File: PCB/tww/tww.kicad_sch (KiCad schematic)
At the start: 53 parts, among them J1 MAINS, J10 Flow|NTC, J11 SPI, J2 WW_Pump, J3 Circ_Pump, J6 FtdiConnector, J9 1Wire Sensors, Q1 BC547, Q2 BC547, SW1 Reset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

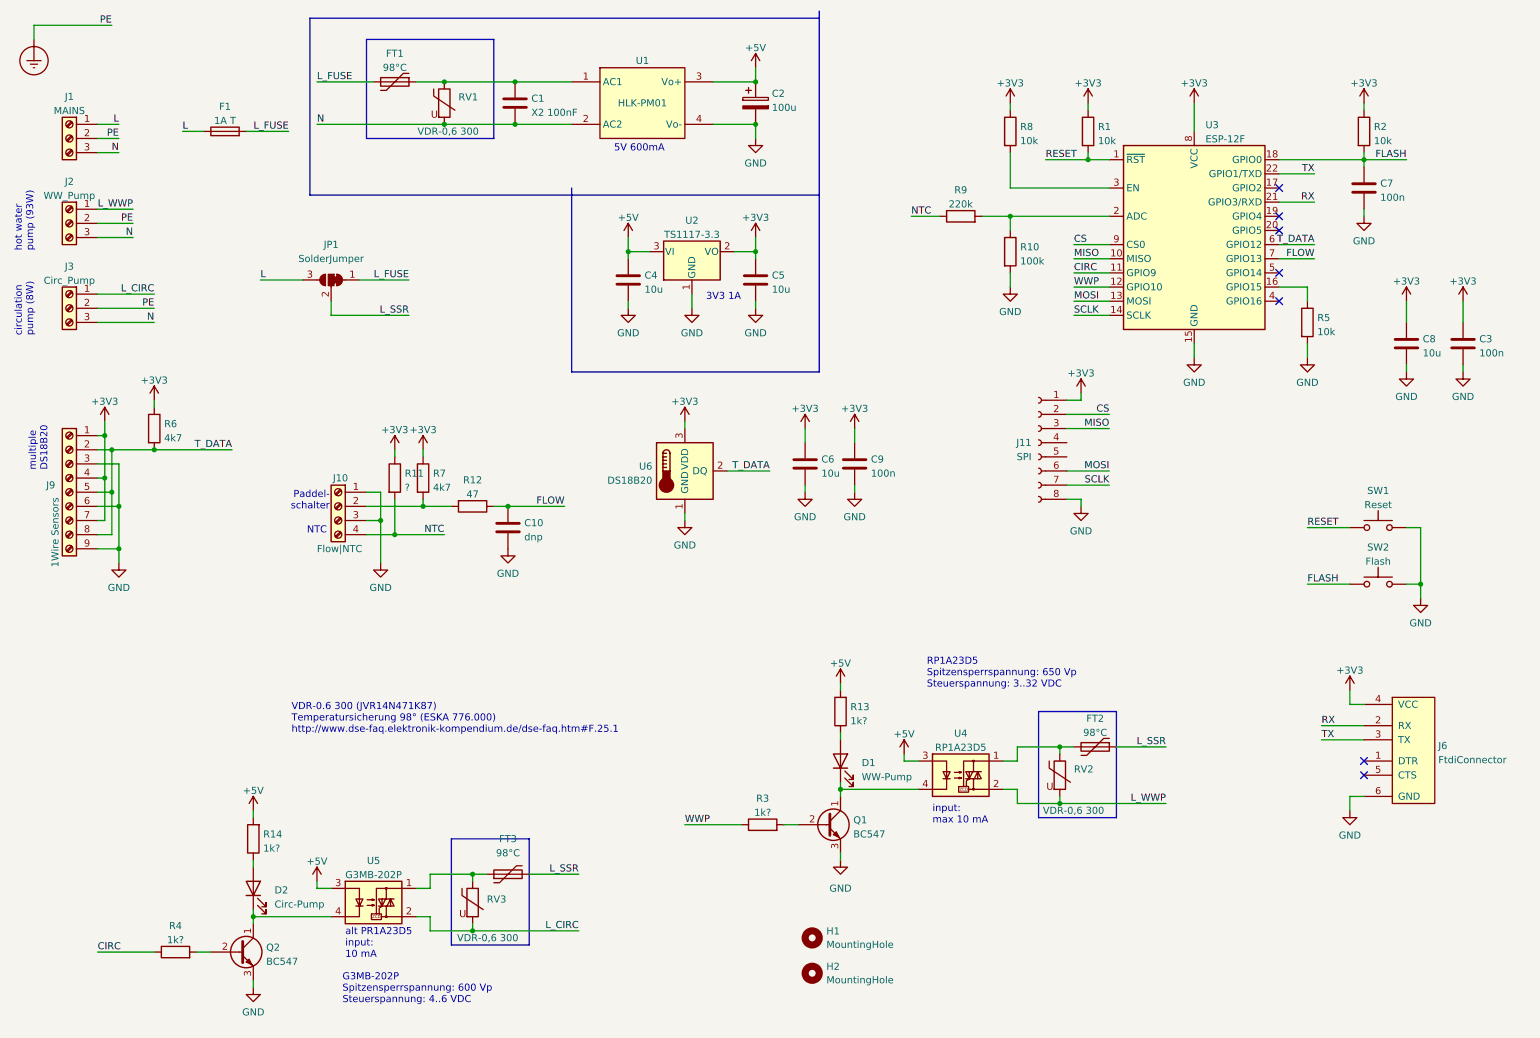
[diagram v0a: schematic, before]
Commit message: update to PCB v1.1
addresses #1

- U1 (HLK-PM01) output polarity swapped
- J6 (FtdiConnector): RX and TX swapped
- J10 label fixed
- VDR-0.6 footprint changed
- replaced BC547 by FET IRLML6344
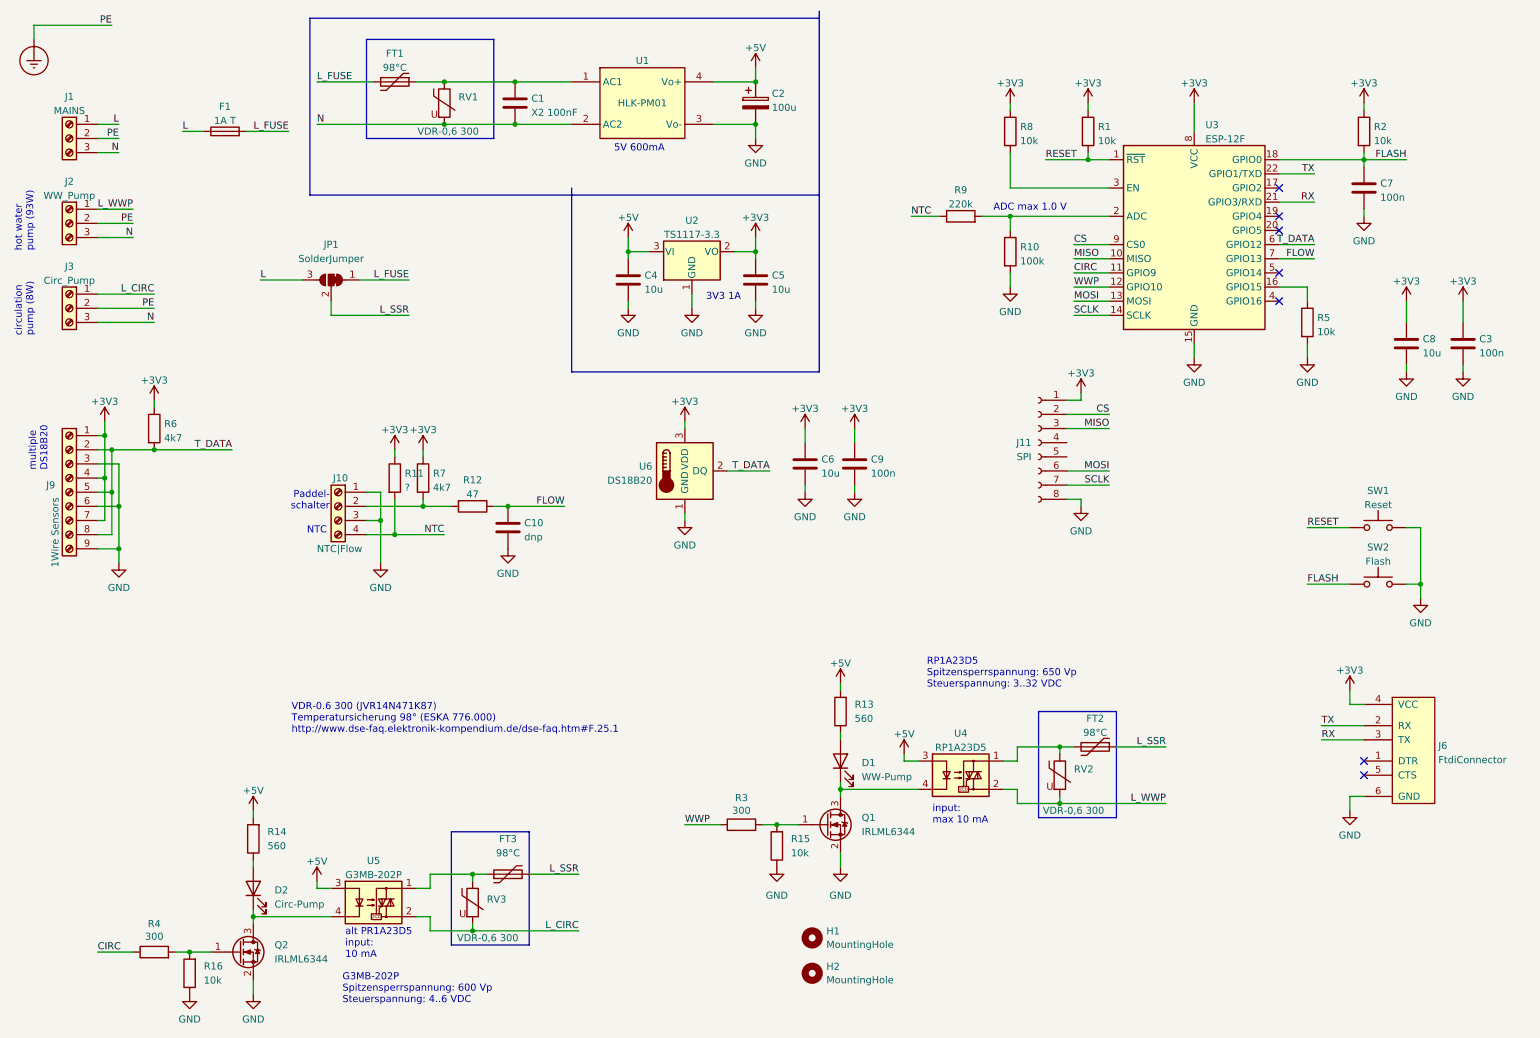
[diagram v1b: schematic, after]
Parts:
- removed Q1, Q2: BC547, Package_TO_SOT_THT:TO-92_Inline, symbol Transistor_BJT:BC547
- added Q1, Q2: IRLML6344, Package_TO_SOT_SMD:SOT-23_Handsoldering, symbol Transistor_FET:IRLML2060
- added R15, R16: 10k, Resistor_SMD:R_0805_2012Metric_Pad1.20x1.40mm_HandSolder, symbol Device:R
- J10: value Flow|NTC -> NTC|Flow
- R13, R14: value 1k? -> 560
- R3, R4: value 1k? -> 300
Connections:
- net +5V: now also U1.4 (Vo+); no longer U1.3 (Vo+)
- net GND: now also U1.3 (Vo-), Q1.2 (S), Q2.2 (S), R15.1, R16.1; no longer U1.4 (Vo-)
- net RX: now also J6.3 (TX); no longer J6.2 (RX)
- net TX: now also J6.2 (RX); no longer J6.3 (TX)
- net at D1.1 (K), U4.4: now also Q1.3 (D)
- net at R3.2: now also Q1.1 (G), R15.2
- net at D2.1 (K), U5.4: now also Q2.3 (D)
- net at R4.2: now also Q2.1 (G), R16.2
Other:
- note added: "ADC max 1.0 V"
- moved on the sheet: R3, R4

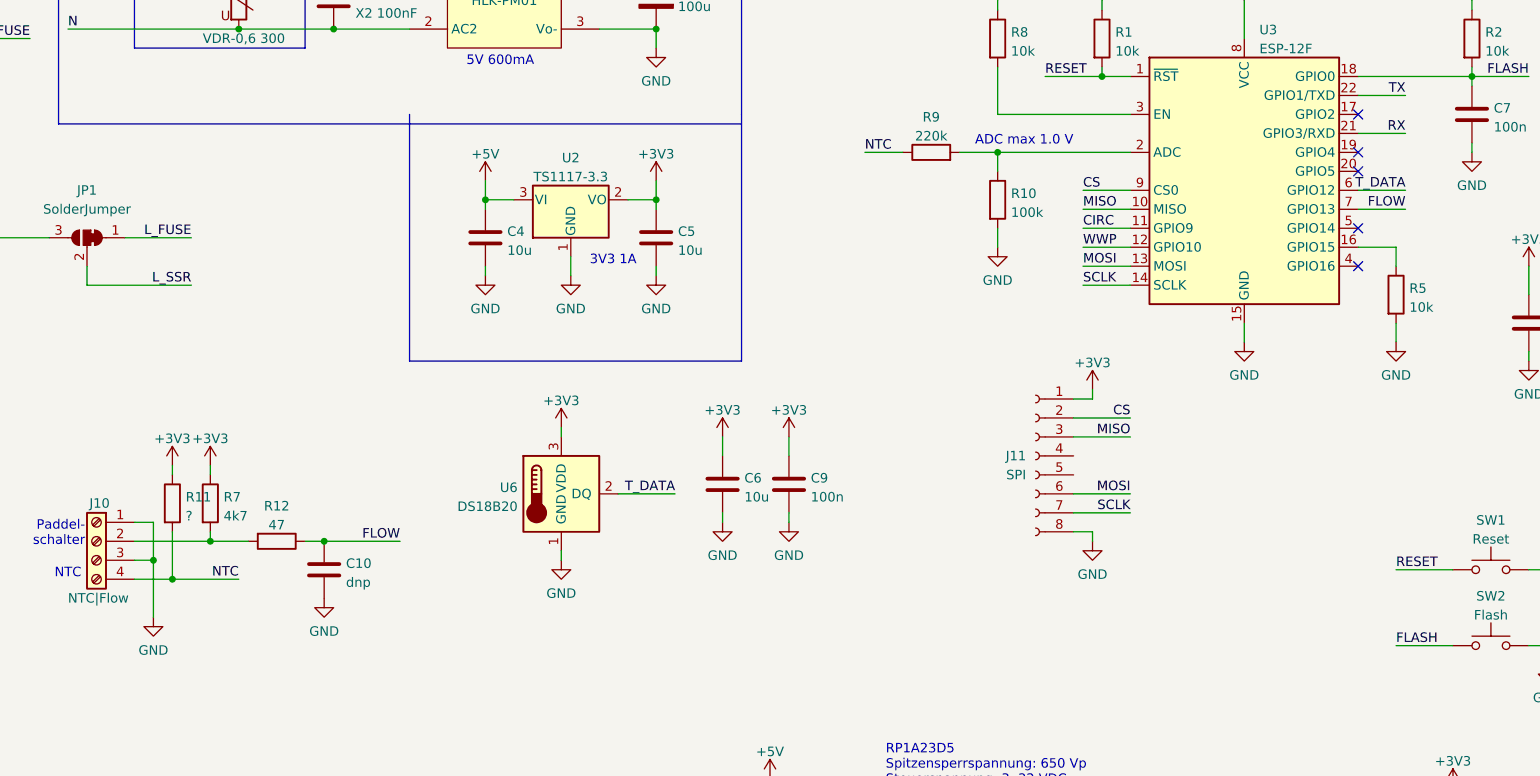
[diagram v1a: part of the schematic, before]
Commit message: updates for PCB version 1.1
- reconnect WWP and CIRC outputs
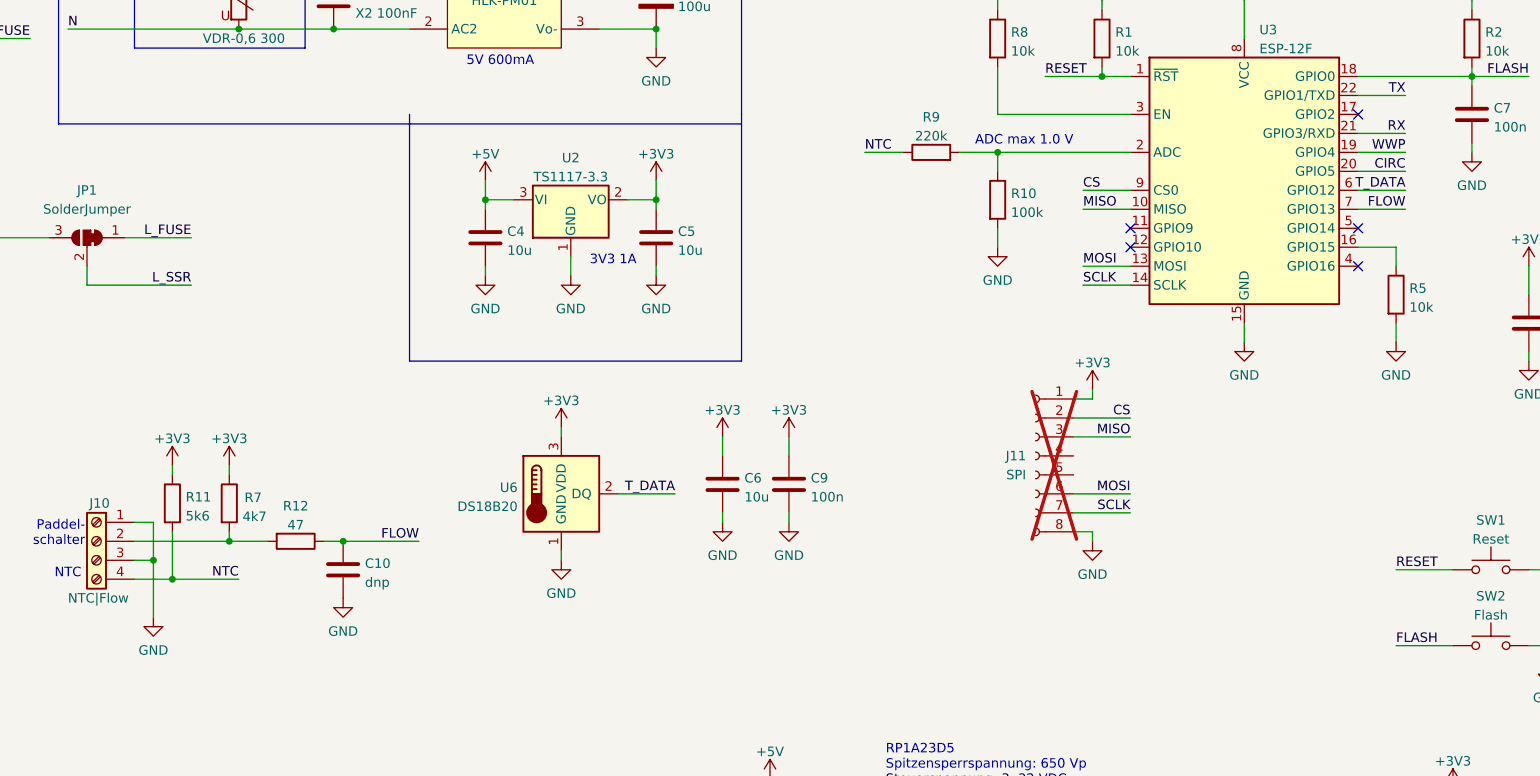
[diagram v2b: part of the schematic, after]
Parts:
- J11: now not fitted
- R11: value ? -> 5k6
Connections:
- net CIRC: now also U3.20 (GPIO5); no longer U3.11 (GPIO9)
- net WWP: now also U3.19 (GPIO4); no longer U3.12 (GPIO10)
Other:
- moved on the sheet: C10, R12, R7
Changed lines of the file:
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@@
 	(title_block
 		(title "TWW - Trinkwarmwasser")
-		(date "2024-10-22")
+		(date "2024-11-15")
 		(rev "1.1")
 		(comment 1 "CC BY-NC-SA 4.0")
@@
 	)
 	(junction
-		(at 104.14 104.14)
+		(at 106.68 104.14)
 		(diameter 0)
 		(color 0 0 0 0)
@@
 	)
 	(junction
+		(at 91.44 104.14)
+		(diameter 0)
+		(color 0 0 0 0)
+	)
+	(junction
 		(at 148.59 35.56)
 		(diameter 0)
@@
 	)
 	(junction
-		(at 88.9 104.14)
-		(diameter 0)
-		(color 0 0 0 0)
-	)
-	(junction
 		(at 34.29 111.76)
 		(diameter 0)
@@
 	)
 	(no_connect
-		(at 242.57 54.61)
-	)
-	(no_connect
 		(at 257.81 152.4)
 	)
@@
 	)
 	(no_connect
-		(at 242.57 52.07)
+		(at 242.57 67.31)
 	)
 	(no_connect
-		(at 242.57 67.31)
+		(at 212.09 62.23)
 	)
 	(no_connect
@@
 		(at 242.57 46.99)
 	)
+	(no_connect
+		(at 212.09 64.77)
+	)
 	(wire
 		(pts
@@
 	(wire
 		(pts
-			(xy 205.74 62.23) (xy 212.09 62.23)
-		)
-		(stroke
-			(width 0)
-			(type default)
-		)
-	)
-	(wire
-		(pts
 			(xy 195.58 157.48) (xy 203.2 157.48)
 		)
@@
 	(wire
 		(pts
+			(xy 242.57 54.61) (xy 248.92 54.61)
+		)
+		(stroke
+			(width 0)
+			(type default)
+		)
+	)
+	(wire
+		(pts
 			(xy 97.79 170.18) (xy 100.33 170.18)
 		)
@@
 	(wire
 		(pts
-			(xy 205.74 64.77) (xy 212.09 64.77)
-		)
-		(stroke
-			(width 0)
-			(type default)
-		)
-	)
-	(wire
-		(pts
 			(xy 257.81 40.64) (xy 257.81 41.91)
 		)
@@
 	(wire
 		(pts
-			(xy 88.9 104.14) (xy 88.9 102.87)
+			(xy 91.44 104.14) (xy 91.44 102.87)
 		)
 		(stroke
@@
 	(wire
 		(pts
-			(xy 101.6 104.14) (xy 104.14 104.14)
+			(xy 104.14 104.14) (xy 106.68 104.14)
 		)
 		(stroke
@@
 	(wire
 		(pts
-			(xy 88.9 104.14) (xy 93.98 104.14)
-		)
-		(stroke
-			(width 0)
-			(type default)
-		)
-	)
-	(wire
-		(pts
 			(xy 242.57 57.15) (xy 248.92 57.15)
 		)
@@
 	(wire
 		(pts
-			(xy 88.9 93.98) (xy 88.9 95.25)
+			(xy 91.44 93.98) (xy 91.44 95.25)
 		)
 		(stroke
@@
 	(wire
 		(pts
+			(xy 242.57 52.07) (xy 248.92 52.07)
+		)
+		(stroke
+			(width 0)
+			(type default)
+		)
+	)
+	(wire
+		(pts
 			(xy 247.65 74.93) (xy 247.65 77.47)
 		)
@@
 	(wire
 		(pts
+			(xy 91.44 104.14) (xy 96.52 104.14)
+		)
+		(stroke
+			(width 0)
+			(type default)
+		)
+	)
+	(wire
+		(pts
 			(xy 30.48 93.98) (xy 33.02 93.98)
 		)
@@
 	(wire
 		(pts
-			(xy 104.14 104.14) (xy 114.3 104.14)
+			(xy 106.68 104.14) (xy 116.84 104.14)
 		)
 		(stroke
@@
 	(wire
 		(pts
-			(xy 78.74 104.14) (xy 88.9 104.14)
+			(xy 78.74 104.14) (xy 91.44 104.14)
 		)
 		(stroke
@@
 	)
 	(label "CIRC"
-		(at 205.74 62.23 0)
+		(at 248.92 54.61 180)
 		(fields_autoplaced yes)
 		(effects
@@
 				(size 1.27 1.27)
 			)
-			(justify left bottom)
+			(justify right bottom)
 		)
 	)
@@
 	)
 	(label "FLOW"
-		(at 114.3 104.14 180)
+		(at 116.84 104.14 180)
 		(fields_autoplaced yes)
 		(effects
@@
 	)
 	(label "WWP"
-		(at 205.74 64.77 0)
+		(at 248.92 52.07 180)
 		(fields_autoplaced yes)
 		(effects
@@
 				(size 1.27 1.27)
 			)
-			(justify left bottom)
+			(justify right bottom)
 		)
 	)
@@
 	(symbol
 		(lib_id "power:GND")
-		(at 104.14 111.76 0)
+		(at 106.68 111.76 0)
 		(unit 1)
 		(exclude_from_sim no)
@@
 		(fields_autoplaced yes)
 		(property "Reference" "#PWR033"
-			(at 104.14 118.11 0)
+			(at 106.68 118.11 0)
 			(effects
 				(font
@@
 		)
 		(property "Value" "GND"
-			(at 104.14 116.2034 0)
+			(at 106.68 116.2034 0)
 			(effects
 				(font
@@
 		)
 		(property "Footprint" ""
-			(at 104.14 111.76 0)
+			(at 106.68 111.76 0)
 			(effects
 				(font
@@
 		)
 		(property "Datasheet" ""
-			(at 104.14 111.76 0)
+			(at 106.68 111.76 0)
 			(effects
 				(font
@@
 		)
 		(property "Description" ""
-			(at 104.14 111.76 0)
+			(at 106.68 111.76 0)
 			(effects
 				(font
@@
 	(symbol
 		(lib_id "Device:C")
-		(at 104.14 107.95 0)
+		(at 106.68 107.95 0)
 		(unit 1)
 		(exclude_from_sim no)
@@
 		(dnp no)
 		(property "Reference" "C10"
-			(at 107.061 107.1153 0)
+			(at 109.601 107.1153 0)
 			(effects
 				(font
@@
 		)
 		(property "Value" "dnp"
-			(at 107.061 109.6522 0)
+			(at 109.601 109.6522 0)
 			(effects
 				(font
@@
 		)
 		(property "Footprint" "Capacitor_SMD:C_0805_2012Metric_Pad1.18x1.45mm_HandSolder"
-			(at 105.1052 111.76 0)
+			(at 107.6452 111.76 0)
 			(effects
 				(font
@@
 		)
 		(property "Datasheet" "~"
-			(at 104.14 107.95 0)
+			(at 106.68 107.95 0)
 			(effects
 				(font
@@
 		)
 		(property "Description" ""
-			(at 104.14 107.95 0)
+			(at 106.68 107.95 0)
 			(effects
 				(font
@@
 			)
 		)
-		(property "Value" "?"
+		(property "Value" "5k6"
 			(at 85.598 100.7622 0)
 			(effects
@@
 	(symbol
 		(lib_id "power:+3V3")
-		(at 88.9 93.98 0)
+		(at 91.44 93.98 0)
 		(unit 1)
 		(exclude_from_sim no)
@@
 		(fields_autoplaced yes)
 		(property "Reference" "#PWR0104"
-			(at 88.9 97.79 0)
+			(at 91.44 97.79 0)
 			(effects
 				(font
@@
 		)
 		(property "Value" "+3V3"
-			(at 88.9 90.4042 0)
+			(at 91.44 90.4042 0)
 			(effects
 				(font
@@
 		)
 		(property "Footprint" ""
-			(at 88.9 93.98 0)
+			(at 91.44 93.98 0)
 			(effects
 				(font
@@
 		)
 		(property "Datasheet" ""
-			(at 88.9 93.98 0)
+			(at 91.44 93.98 0)
 			(effects
 				(font
@@
 		)
 		(property "Description" ""
-			(at 88.9 93.98 0)
+			(at 91.44 93.98 0)
 			(effects
 				(font
@@
 		(in_bom yes)
 		(on_board yes)
-		(dnp no)
+		(dnp yes)
 		(property "Reference" "J11"
 			(at 198.12 92.7099 0)
@@
 	(symbol
 		(lib_id "Device:R")
-		(at 97.79 104.14 270)
+		(at 100.33 104.14 270)
 		(unit 1)
 		(exclude_from_sim no)
@@
 		(dnp no)
 		(property "Reference" "R12"
-			(at 97.79 99.4242 90)
+			(at 100.33 99.4242 90)
 			(effects
 				(font
@@
 		)
 		(property "Value" "47"
-			(at 97.79 101.9611 90)
+			(at 100.33 101.9611 90)
 			(effects
 				(font
@@
 		)
 		(property "Footprint" "Resistor_SMD:R_0805_2012Metric_Pad1.20x1.40mm_HandSolder"
-			(at 97.79 102.362 90)
+			(at 100.33 102.362 90)
 			(effects
 				(font
@@
 		)
 		(property "Datasheet" "~"
-			(at 97.79 104.14 0)
+			(at 100.33 104.14 0)
 			(effects
 				(font
@@
 		)
 		(property "Description" ""
-			(at 97.79 104.14 0)
+			(at 100.33 104.14 0)
 			(effects
 				(font
@@
 	(symbol
 		(lib_id "Device:R")
-		(at 88.9 99.06 0)
+		(at 91.44 99.06 0)
 		(unit 1)
 		(exclude_from_sim no)
@@
 		(dnp no)
 		(property "Reference" "R7"
-			(at 90.678 98.2253 0)
+			(at 93.472 98.298 0)
 			(effects
 				(font
@@
 		)
 		(property "Value" "4k7"
-			(at 90.678 100.7622 0)
+			(at 93.218 100.838 0)
 			(effects
 				(font
@@
 		)
 		(property "Footprint" "Resistor_SMD:R_0805_2012Metric_Pad1.20x1.40mm_HandSolder"
-			(at 87.122 99.06 90)
+			(at 89.662 99.06 90)
 			(effects
 				(font
@@
 		)
 		(property "Datasheet" "~"
-			(at 88.9 99.06 0)
+			(at 91.44 99.06 0)
 			(effects
 				(font
@@
 		)
 		(property "Description" ""
-			(at 88.9 99.06 0)
+			(at 91.44 99.06 0)
 			(effects
 				(font
